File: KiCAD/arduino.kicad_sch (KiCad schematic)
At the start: 3 parts, among them J5 ENC_INT, U2 Metro_ESP32S3

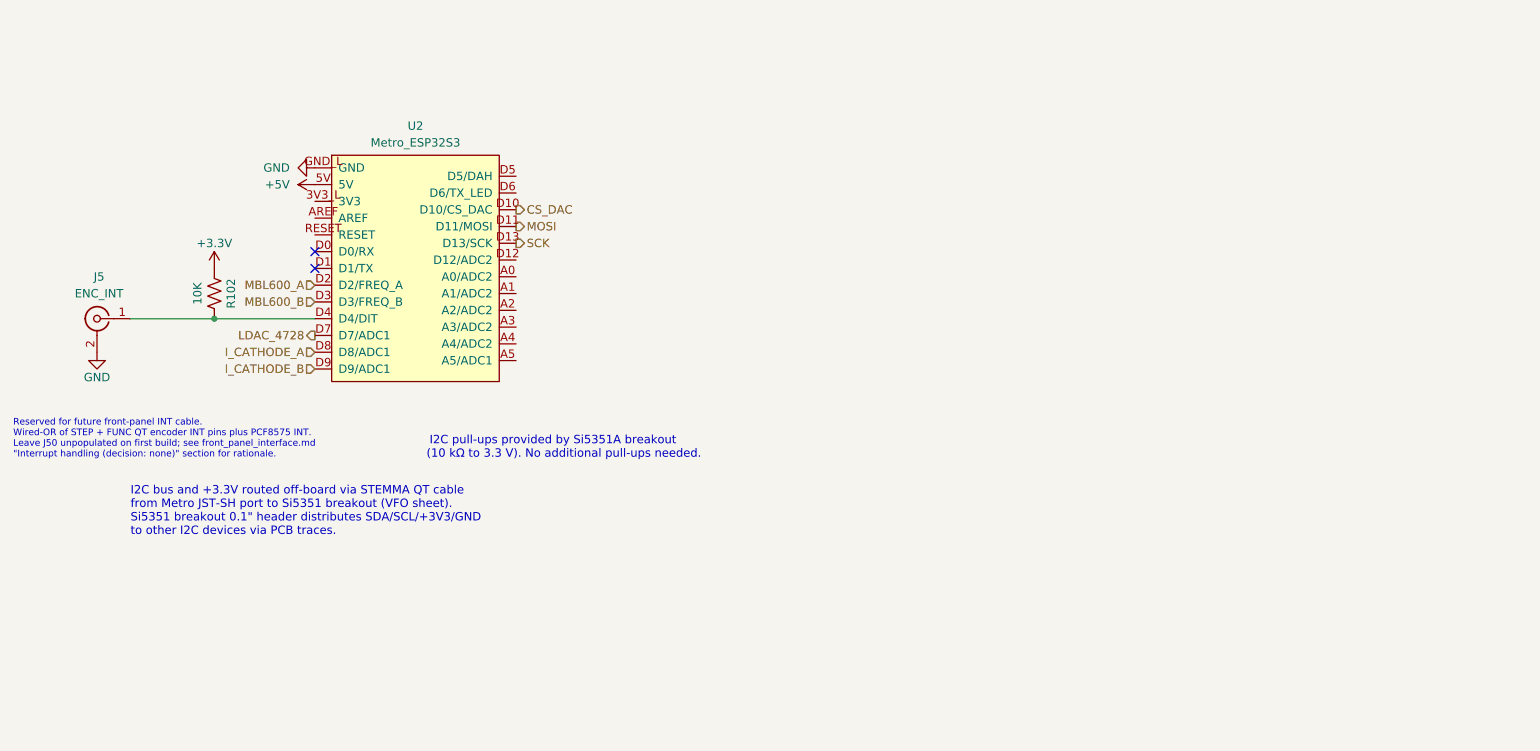
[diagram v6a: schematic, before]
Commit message: arduino: main-board PCF8575 at 0x21 + relay drivers + TR_SENSE
Adds the second PCF8575 breakout (U17) on the main board at I2C address
0x21 (A0 jumper closed), giving 16 GPIO for relay drivers and other
non-time-critical control outputs. Wired to the shared I2C bus via
SDA/SCL hierarchical labels at U17's I2C pins. Bypass caps C36 (100 nF)
and C37 (10 uF) local to the PCF8575.

Two 2N7000 low-side relay drivers Q4, Q5 with 2-pin connectors J6 and
J7 for off-PCB relays:
  - J6: Transmit/Receive relay coil (main T/R switching, DPDT --
    second pole provides TR_SENSE confirmation)
  - J7: High Voltage Primary Relay coil (gates the HV supply)
  - Each relay coil requires a 1N4001 flyback diode at the coil end.
  - Still to add: third driver + connector for the HV in-rush limiter
    bypass relay.

TR_SENSE confirmation input:
  - J8 is a 2-pin connector for the DPDT T/R relay's second-pole
    contacts. Pin 1 to +3.3V (NC contact -- RX idle state = HIGH).
    Pin 2 to Metro A5 via C38 (100 nF RF filter cap right at the
    connector entry). The NO contact is wired to GND at the relay
    itself, so activated (TX) state pulls A5 to LOW. Firmware waits
    for the falling edge before enabling PA drive.

GRID_BLOCK_CRASH hierarchical input label added at Metro D12 so
firmware can log cathode-monitor faults to NVS.

I_CATHODE_A and I_CATHODE_B moved from A0 / A1 (ADC2) to D8 / D9
(ADC1) -- honors the WiFi/BLE-on-ADC2 concern from the cathode-monitor
design decision.

Still pending on this sheet (per Documentation/design_review_7-5-26.md):
paddle inputs on D5 / D6; third relay driver for HV in-rush bypass;
text-note cleanup on J8 role and stale J50 reference.

Co-Authored-By: Claude Opus 4.7 <noreply@anthropic.com>
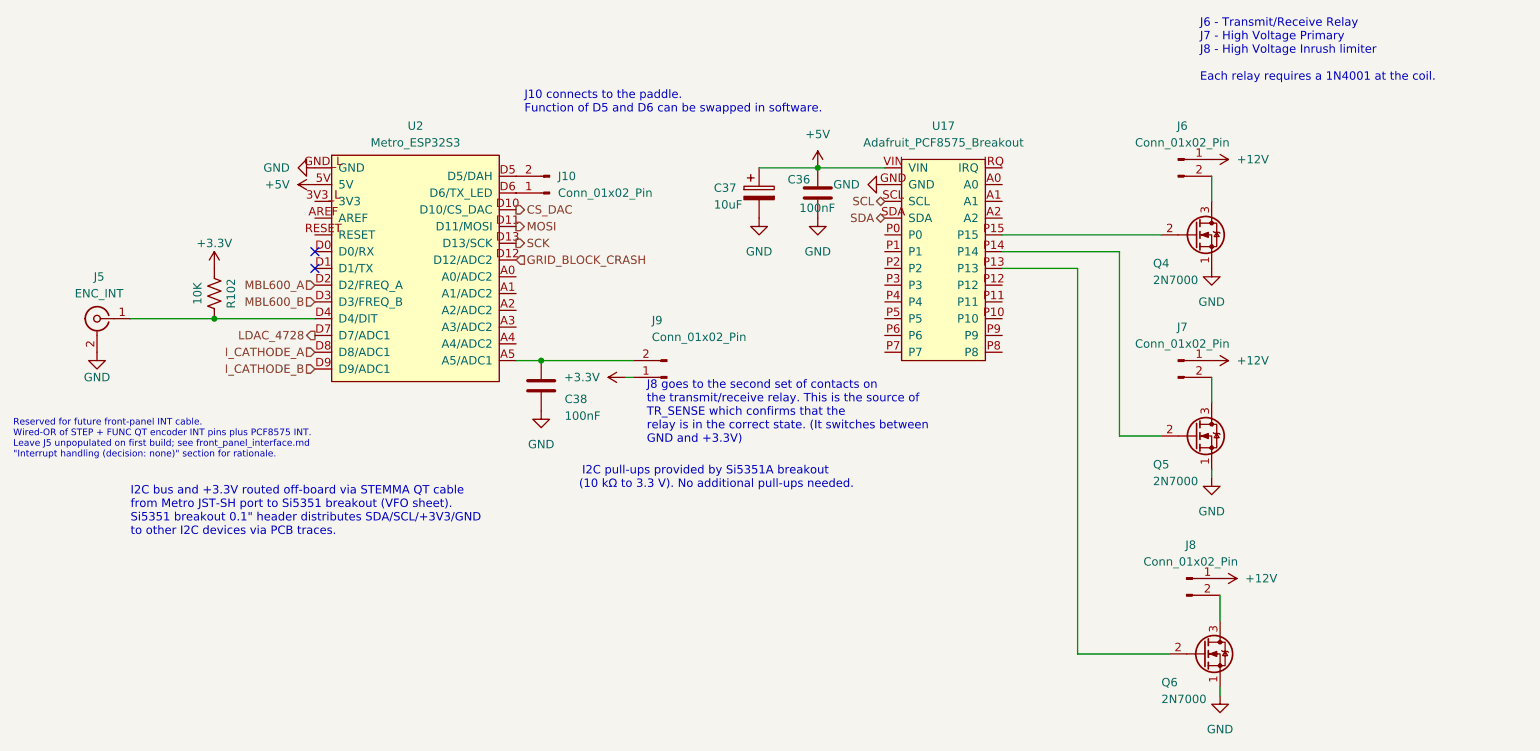
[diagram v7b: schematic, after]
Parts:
- added C36, C38: 100nF, symbol Device:C
- added C37: 10uF, symbol Device:C_Polarized
- added J10, J6, J7, J8, J9: Conn_01x02_Pin, symbol Connector:Conn_01x02_Pin
- added Q4, Q5, Q6: 2N7000, Package_TO_SOT_THT:TO-92_Inline, symbol Transistor_FET:2N7000
- added U17: Adafruit_PCF8575_Breakout, xmitter:Adafruit_PCF8575_Breakout, symbol xmitter:Adafruit_PCF8575_Breakout
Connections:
- net +3.3V: now also J9.1 (Pin_1)
- net +5V: now also C36.1, C37.1, U17.VIN
- net GND: now also C36.2, C37.2, C38.2, Q4.1 (S), Q5.1 (S), Q6.1 (S), U17.GND
- net at U2.A5 (A5/ADC1): now also C38.1, J9.2 (Pin_2)
- net GRID_BLOCK_CRASH: now reaches U2.D12 (D12/ADC2)
- net at U2.D5 (D5/DAH): now also J10.2 (Pin_2)
- net at U2.D6 (D6/TX_LED): now also J10.1 (Pin_1)
- new net: J7.2 (Pin_2), Q5.3 (D)
- new net: Q6.2 (G), U17.P13
- new net: Q5.2 (G), U17.P14
- new net: Q4.2 (G), U17.P15
- new net: J6.2 (Pin_2), Q4.3 (D)
- new net: J8.2 (Pin_2), Q6.3 (D)
- new net +12V: J6.1 (Pin_1), J7.1 (Pin_1), J8.1 (Pin_1)
- new net SCL: U17.SCL
- new net SDA: U17.SDA
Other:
- note added: "J10 connects to the paddle. Function of D5 and D6 can be swapped in software."
- note added: "J6 - Transmit/Receive Relay J7 - High Voltage Primary J8 - High Voltage Inrush limiter Each relay requires a 1N4001 at the coil."
- note added: "J8 goes to the second set of contacts on the transmit/receive relay. This is the source of TR_SENSE which confirms that the relay is in the correct state. (It switches between GND and +3.3V)"
- note added: "Reserved for future front-panel INT cable. Wired-OR of STEP + FUNC QT encoder INT pins plus PCF8575 INT. Leave J5 unpopulated on first build; see front_panel_interface.md "Interrupt handling (decision: none)" section for rationale."
- note removed: "Reserved for future front-panel INT cable. Wired-OR of STEP + FUNC QT encoder INT pins plus PCF8575 INT. Leave J50 unpopulated on first build; see front_panel_interface.md "Interrupt handling (decision: none)" section for rationale."

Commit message: kicad: fill missing footprints across active sheets + MCP4728 breakout footprint
Footprint sweep across the analog control board sheets. All active sheets
now clean except U2 (Metro), which is intentionally off-PCB per the
Wingshield-plus-jumpers connection strategy.

Auto-assigned via tools/assign_cap_footprints.py:
  - buffer_keyer: C39, C40 (100 nF, THT disc D5.0mm P5.00mm) -- the null-
    trim bypass caps at R_INJ1 / R_INJ2 that ground the DAC output side
    of the 330K injection resistors going into T1 and T2
  - arduino: C36, C38 (100 nF THT disc), C37 (10 uF radial electrolytic)
  - interface: C34 (100 nF), C35 (10 uF)

Manual assignments:
  - interface: R26, R27, R28, R29 -> R_Axial_DIN0207_L6.3mm axial THT
    (matching the other 1/4W metal-film resistors used throughout)
  - interface: J4 (RJ45 socket) -> xmitter:Amphenol_RJE1D-188_Horizontal_Shielded
  - arduino: J6, J7, J8, J9, J10 -> PinHeader_1x02_P2.54mm_Vertical
  - buffer_keyer: U8 (MCP4728 breakout) -> new custom footprint

New custom footprint xmitter:Adafruit_MCP4728_Breakout:
  - Board 1.00 x 0.70 in (25.4 x 17.78 mm)
  - Four NPTH 2.5 mm mounting holes on 0.80 x 0.50 in spacing
  - 10 THT pads in two rows of 5, pad numbers match the xmitter:MCP4728
    symbol (1=VIN, 2=GND, 3=SCL, 4=SDA, 5=LDAC, 6=RDY, 7=VA, 8=VB, 9=VC,
    10=VD)
  - Pins 3 (SCL) and 4 (SDA) will be left unrouted on the parent PCB
    per the STEMMA QT daisy-chain topology decision -- I2C reaches the
    MCP4728 via a STEMMA cable from the Si5351 breakout, not via PCB
    traces
  - descr field flags "VERIFY silk-label to pad-number correspondence
    against the physical breakout before routing" -- Adafruit revisions
    vary and the specific row assignment was inferred from the
    datasheet fab print on page 20 plus the symbol pin numbering

Also committing Documentation/Components/MCP4728_datasheet.pdf and
Documentation/Components/cd4050b.pdf datasheets that were sitting
uncommitted.

Co-Authored-By: Claude Opus 4.7 <nor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
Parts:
- C36, C38: footprint (none) -> Capacitor_THT:C_Disc_D5.0mm_W2.5mm_P5.00mm
- C37: footprint (none) -> Capacitor_THT:CP_Radial_D5.0mm_P2.00mm
- J10, J6, J7, J8, J9: footprint (none) -> Connector_PinHeader_2.54mm:PinHeader_1x02_P2.54mm_Vertical
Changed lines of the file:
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@@
 			)
 		)
-		(property "Footprint" ""
+		(property "Footprint" "Connector_PinHeader_2.54mm:PinHeader_1x02_P2.54mm_Vertical"
 			(at 219.71 87.63 0)
 			(hide yes)
@@
 			)
 		)
-		(property "Footprint" ""
+		(property "Footprint" "Capacitor_THT:C_Disc_D5.0mm_W2.5mm_P5.00mm"
 			(at 166.0652 66.04 0)
 			(hide yes)
@@
 			)
 		)
-		(property "Footprint" ""
+		(property "Footprint" "Connector_PinHeader_2.54mm:PinHeader_1x02_P2.54mm_Vertical"
 			(at 124.46 62.23 0)
 			(hide yes)
@@
 			)
 		)
-		(property "Footprint" ""
+		(property "Footprint" "Capacitor_THT:C_Disc_D5.0mm_W2.5mm_P5.00mm"
 			(at 124.1552 95.25 0)
 			(hide yes)
@@
 			)
 		)
-		(property "Footprint" ""
+		(property "Footprint" "Connector_PinHeader_2.54mm:PinHeader_1x02_P2.54mm_Vertical"
 			(at 219.71 57.15 0)
 			(hide yes)
@@
 			)
 		)
-		(property "Footprint" ""
+		(property "Footprint" "Connector_PinHeader_2.54mm:PinHeader_1x02_P2.54mm_Vertical"
 			(at 220.98 120.65 0)
 			(hide yes)
@@
 			)
 		)
-		(property "Footprint" ""
+		(property "Footprint" "Capacitor_THT:CP_Radial_D5.0mm_P2.00mm"
 			(at 157.1752 66.04 0)
 			(hide yes)
@@
 			)
 		)
-		(property "Footprint" ""
+		(property "Footprint" "Connector_PinHeader_2.54mm:PinHeader_1x02_P2.54mm_Vertical"
 			(at 142.24 90.17 0)
 			(hide yes)
